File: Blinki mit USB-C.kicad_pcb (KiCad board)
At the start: 2 copper layers, 32.5 x 57.5 mm, 20 parts, among them J1 USB_C_Receptacle_PowerOnly_6P, Q1 BC337, Q2 BC337

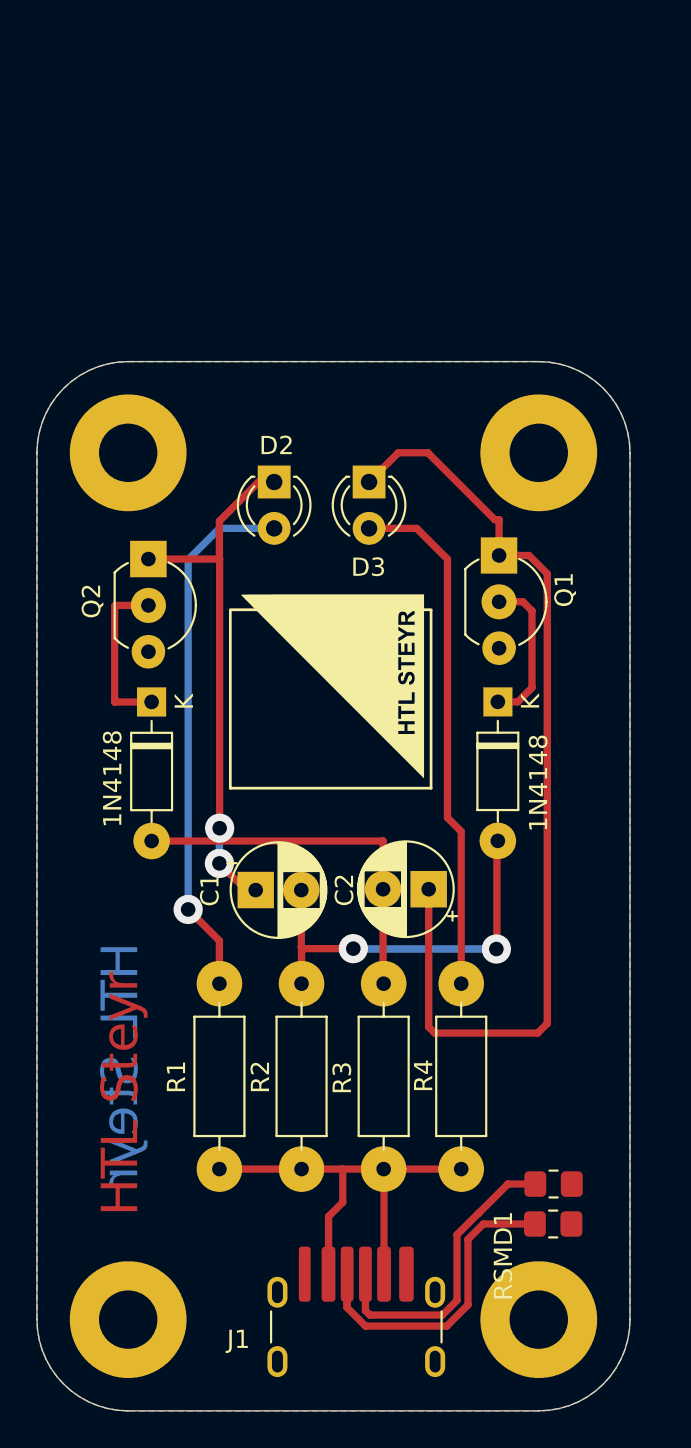
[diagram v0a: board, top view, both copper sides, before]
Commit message: Update Blinki mit USB-C.kicad_pcb
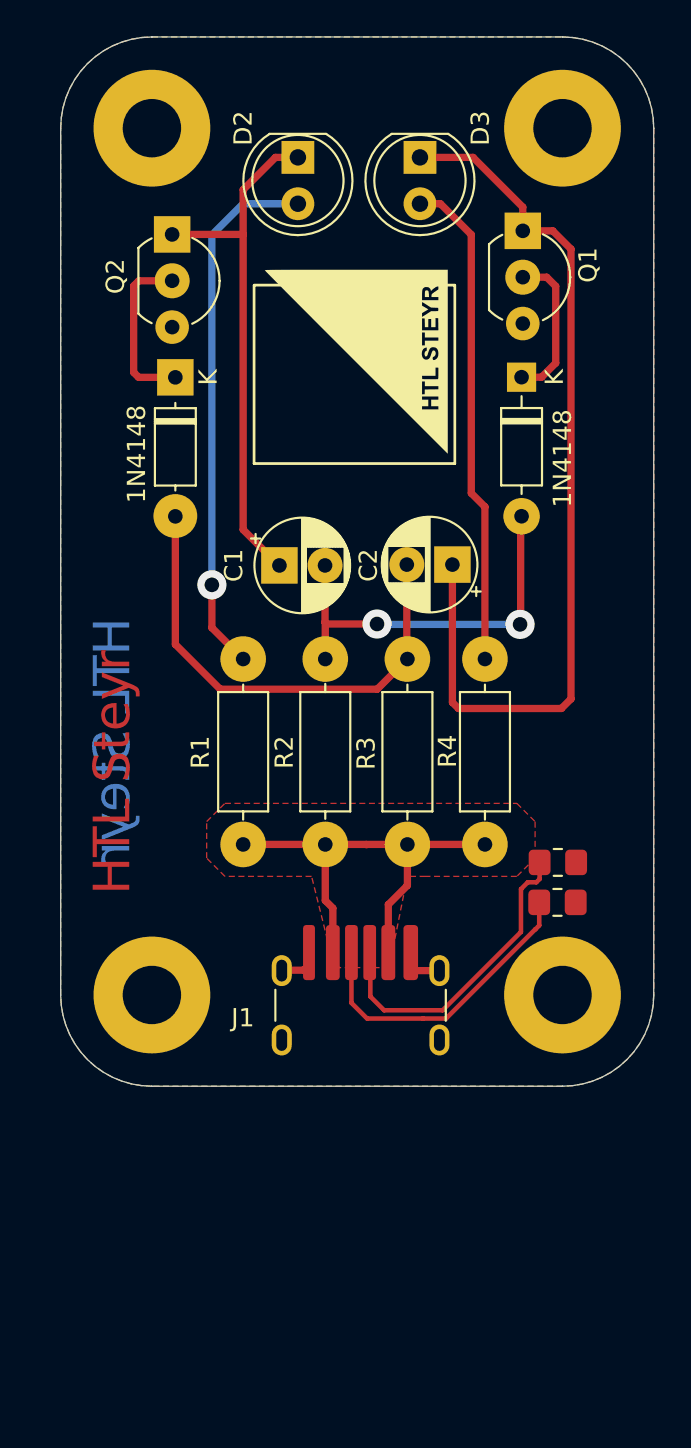
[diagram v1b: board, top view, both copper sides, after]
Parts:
- D2, D3: footprint LED_THT:LED_D3.0mm_FlatTop -> LED_THT:LED_D5.0mm
- moved D3 18.0 mm to (141.0, 68.8)
- moved D4 17.8 mm to (127.6, 80.9)
- moved H1 17.8 mm to (126.3, 67.2)
- moved H2 17.8 mm to (148.8, 67.2)
- moved H3 17.8 mm to (148.8, 114.7)
- moved H4 17.8 mm to (126.3, 114.7)
- moved Q2 17.8 mm to (127.4, 73.0)
- moved R1 17.8 mm to (131.3, 96.3)
- moved R2 17.8 mm to (135.8, 106.5)
- moved R3 17.8 mm to (140.3, 96.3)
- moved R4 17.8 mm to (144.6, 96.3)
- moved C1 17.8 mm to (133.3, 91.2)
- moved C2 17.8 mm to (142.8, 91.1)
- moved D1 17.8 mm to (146.6, 80.9)
- moved D2 17.8 mm to (134.3, 68.8)
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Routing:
- net Net-(D4-A): track 20.5 -> 26.6 mm
- net GND: track 0.49 -> 5.36 mm
- net Net-(D3-K): track 53.4 -> 50.2 mm
- net Net-(D3-A): track 28.6 -> 27.1 mm
- net Net-(J1-CC2): track 16.5 -> 17.3 mm
- net VCC: track 26.2 -> 26.8 mm
- net Net-(D2-K): track 29.3 -> 29.2 mm, vias 2 -> 0
- added copper zone on F.Cu, net VCC
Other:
- board text removed: "${REFERENCE}"
